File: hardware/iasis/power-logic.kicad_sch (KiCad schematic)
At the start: 27 parts, among them U1040 AP3441SHE-7B, U1060 AP3441SHE-7B, U1080 TPS3808G33DBVR

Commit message: Redraw the power input, host power and logic supply sheets
The charging input, host power budget and logic supply sheets follow
the power path left to right: connector and protection, switches and
eFuses, then the converters with their feedback and output capacitors.
Supply rails use power symbols with their existing net names, notes sit
beside their circuits, and each sheet carries a title, date and
revision. The netlist is unchanged.
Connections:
- no-connect marks 5 -> 3
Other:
- title: (none) -> Logic supplies and power-on reset
- moved on the sheet: C1040, C1041, C1042, C1043, C1044, C1045, C1046, C1047, C1060, C1061, C1062, C1063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

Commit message: Raise the core rail setpoint for the plane drop
A DC solve of the routed copper puts the hub's VCORE pins 5.5 to 9.9 mV
and the RP2354's DVDD pins 8.4 to 8.6 mV below the AP3441 feedback tap
at 1.5 A. With R1061 at 11.5k the worst static hub voltage was about
1.092 V against the hub's 1.09 V minimum.

R1061 11.3k (RT0603BRD0711K3L, C861088) puts the tap at 1.131 V
nominal, 1.111 to 1.151 V over tolerance: worst loaded hub about
1.101 V, worst unloaded RP2354 1.151 V against its 1.16 V maximum.
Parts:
- R1061: value 11.5k 0.1% -> 11.3k 0.1%; LCSC C705719 -> C861088; MPN RT0603BRD0711K5L -> RT0603BRD0711K3L
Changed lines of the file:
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@@
 			)
 		)
-		(property "Value" "11.5k 0.1%"
+		(property "Value" "11.3k 0.1%"
 			(at 139.7 124.46 0)
 			(show_name no)
@@
 			)
 		)
-		(property "Datasheet" "https://wmsc.lcsc.com/wmsc/upload/file/pdf/v2/lcsc/2009282238_YAGEO-RT0603BRD0711K5L_C705719.pdf"
+		(property "Datasheet" "https://wmsc.lcsc.com/wmsc/upload/file/pdf/v2/lcsc/2203300930_YAGEO-RT0603BRD0711K3L_C861088.pdf"
 			(at 137.16 123.19 0)
 			(hide yes)
@@
 			)
 		)
-		(property "LCSC" "C705719"
+		(property "LCSC" "C861088"
 			(at 137.16 123.19 0)
 			(hide yes)
@@
 			)
 		)
-		(property "MPN" "RT0603BRD0711K5L"
+		(property "MPN" "RT0603BRD0711K3L"
 			(at 137.16 123.19 0)
 			(hide yes)

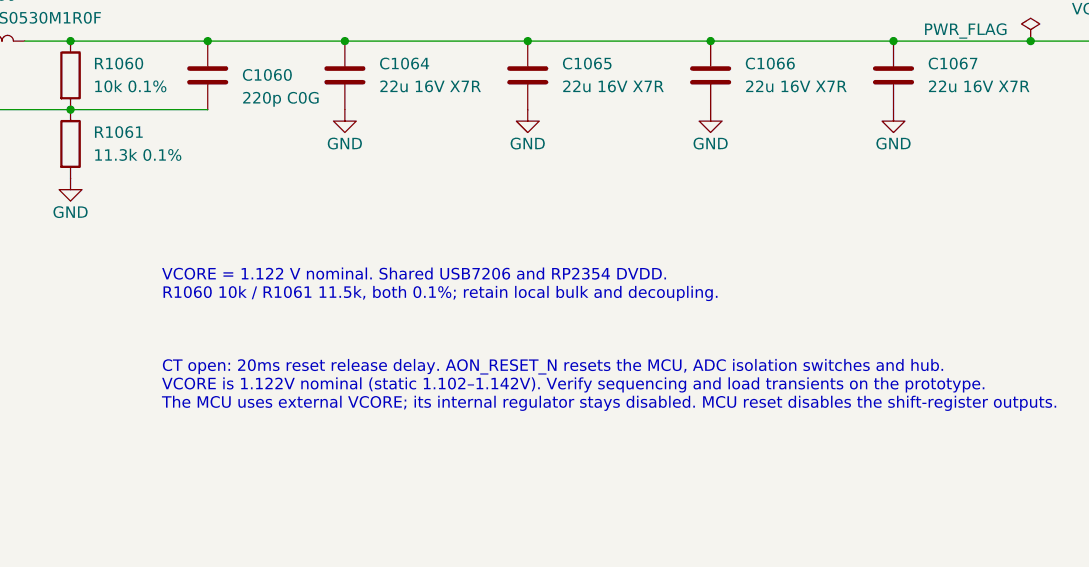
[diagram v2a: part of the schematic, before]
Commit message: fix: correct core power and recovery circuitry
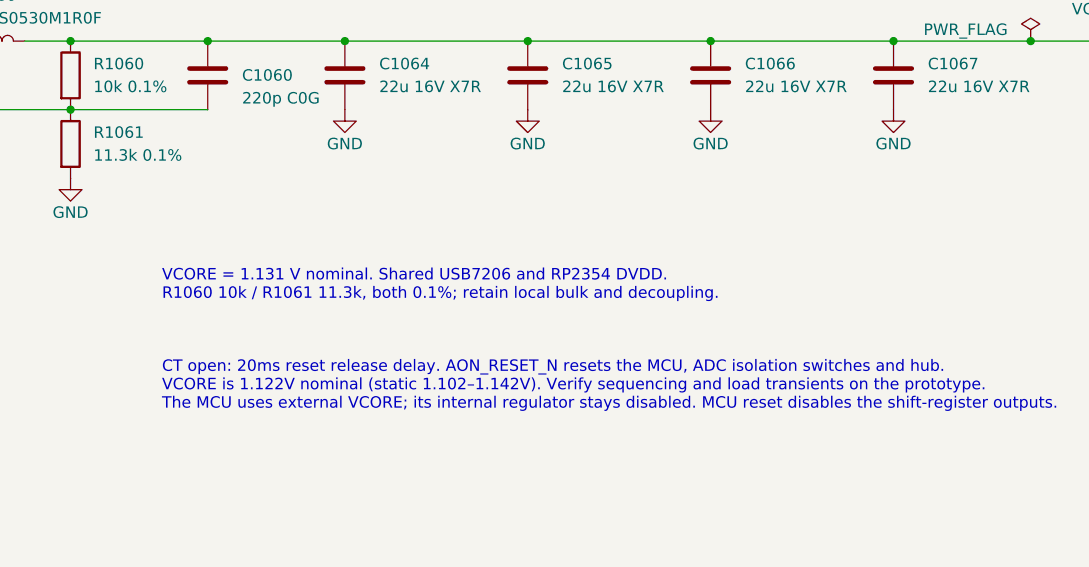
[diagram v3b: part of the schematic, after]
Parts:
- R1061: LCSC C861088 -> C3980906; MPN RT0603BRD0711K3L -> TNPW060311K3BEEA; Manufacturer YAGEO -> Vishay
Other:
- note added: "VCORE = 1.131 V nominal. Shared USB7206 and RP2354 DVDD. R1060 10k / R1061 11.3k, both 0.1%; retain local bulk and decoupling."
- note removed: "VCORE = 1.122 V nominal. Shared USB7206 and RP2354 DVDD. R1060 10k / R1061 11.5k, both 0.1%; retain local bulk and decoupling."
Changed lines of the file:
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@@
 		)
 	)
-	(text "VCORE = 1.122 V nominal. Shared USB7206 and RP2354 DVDD.\nR1060 10k / R1061 11.5k, both 0.1%; retain local bulk and decoupling."
+	(text "VCORE = 1.131 V nominal. Shared USB7206 and RP2354 DVDD.\nR1060 10k / R1061 11.3k, both 0.1%; retain local bulk and decoupling."
 		(exclude_from_sim no)
 		(at 147.32 137.16 0)
@@
 			)
 		)
-		(property "Datasheet" "https://wmsc.lcsc.com/wmsc/upload/file/pdf/v2/lcsc/2203300930_YAGEO-RT0603BRD0711K3L_C861088.pdf"
+		(property "Datasheet" "https://www.vishay.com/docs/28758/tnpw_e3.pdf"
 			(at 137.16 123.19 0)
 			(hide yes)
@@
 			)
 		)
-		(property "LCSC" "C861088"
+		(property "LCSC" "C3980906"
 			(at 137.16 123.19 0)
 			(hide yes)
@@
 			)
 		)
-		(property "MPN" "RT0603BRD0711K3L"
+		(property "MPN" "TNPW060311K3BEEA"
 			(at 137.16 123.19 0)
 			(hide yes)
@@
 			)
 		)
-		(property "Manufacturer" "YAGEO"
+		(property "Manufacturer" "Vishay"
 			(at 137.16 123.19 0)
 			(hide yes)
